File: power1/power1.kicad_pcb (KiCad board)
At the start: 2 copper layers, 40 x 30 mm, 28 parts, among them P1 CONN_01X02, P2 CONN_01X04, U1 LT3633

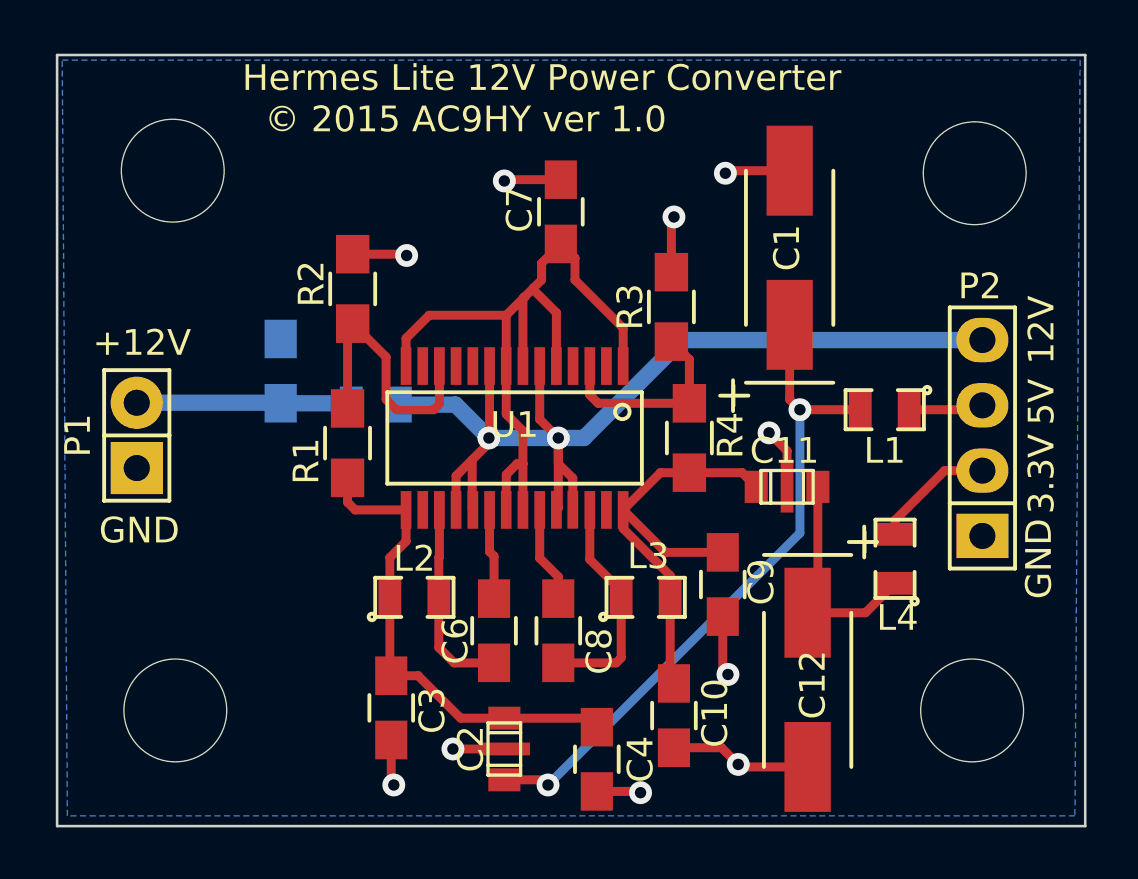
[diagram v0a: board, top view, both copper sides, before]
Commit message: heatsink change
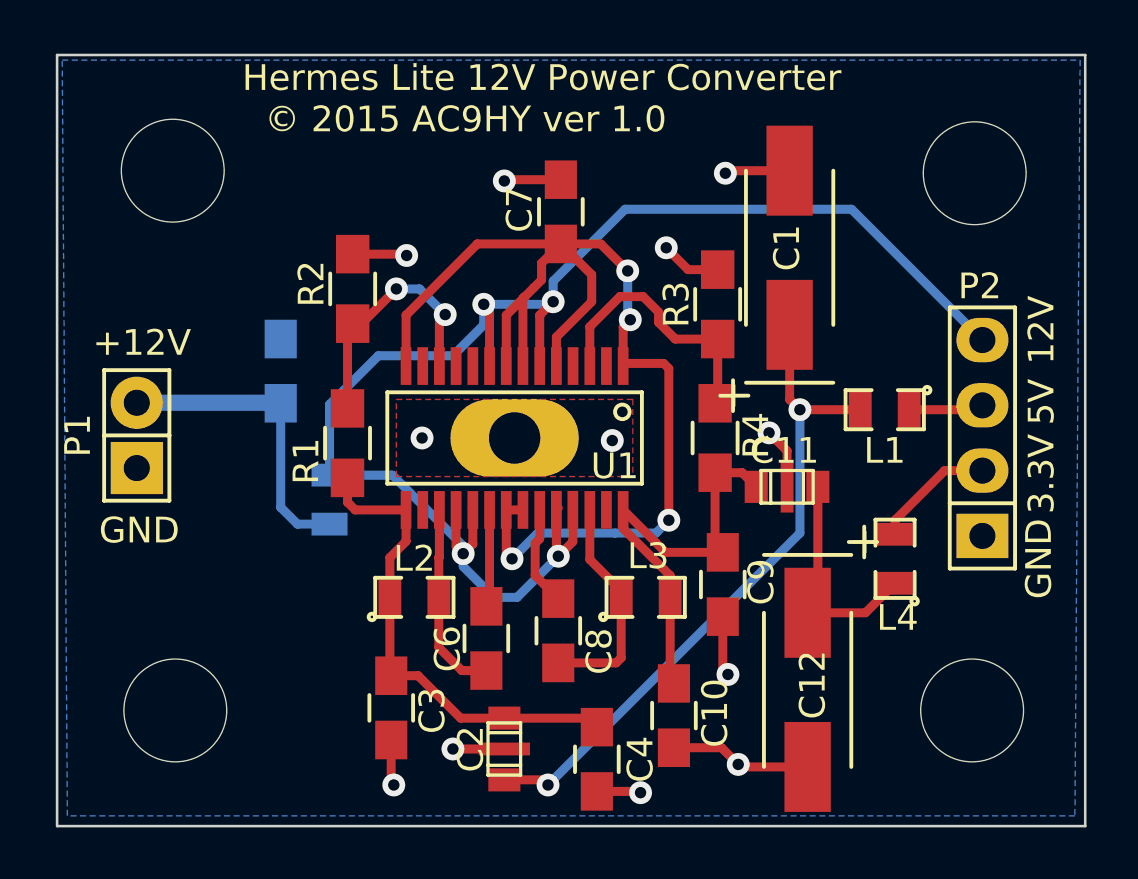
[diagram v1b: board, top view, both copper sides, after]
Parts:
- added TH-OVAL: VAL**, HERMESLITE:TH-OVAL, F.Cu at (141.8, 114.9)
- moved L5 4.11 mm to (134.6, 117.3), turned to 90 degrees
- moved R3 1.80 mm to (149.7, 109.7)
- moved R4 1.00 mm to (149.6, 114.9)
- moved C6 0.42 mm to (140.7, 122.7)
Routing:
- net Net-(L5-Pad2): track 42.0 -> 59.4 mm, vias 2 -> 4
- net Net-(C7-Pad1): track 30.9 -> 48.2 mm, vias 0 -> 4
- net Net-(C5-Pad1): track 8.38 -> 11.8 mm
- net Net-(R3-Pad2): track 7.82 -> 10.4 mm
- net Net-(C10-Pad1): track 18.1 -> 17.2 mm
- net Net-(R1-Pad1): track 10.7 -> 10.1 mm, vias 0 -> 2
- net GND: track 24.8 -> 25.0 mm, vias 10 -> 12
- added copper zone on F.Cu, net GND
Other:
- net class Default: clearance 0.254 -> 0.19812
- rule trace_clearance: 0.254 -> 0.19812

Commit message: More pcb changes
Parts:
- TH-OVAL: footprint HERMESLITE:TH-OVAL -> TH-OVAL
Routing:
- net GND: vias 12 -> 10
- removed copper zone on F.Cu, net GND

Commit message: Few more pcb changes
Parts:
- added C13: DNI, Capacitors_Tantalum_SMD:TantalC_SizeC_EIA-6032_HandSoldering, B.Cu at (150.3, 104.2)
- added C14: DNI, Capacitors_SMD:C_0805_HandSoldering, B.Cu at (156.2, 111.2)
- C5: footprint Capacitors_SMD:C_0805_HandSoldering -> Capacitors_Tantalum_SMD:TantalC_SizeC_EIA-6032_HandSoldering
- moved L5 1.80 mm to (134.6, 119.1), turned to 0 degrees
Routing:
- net Net-(C13-Pad1): track 59.5 -> 65.1 mm
- net Net-(C5-Pad1): track 11.8 -> 10.3 mm
